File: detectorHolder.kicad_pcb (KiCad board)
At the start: 2 copper layers, 58.8 x 83 mm, 46 parts, among them J1 Conn_01x03, J2 Conn_02x02_Odd_Even

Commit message: PCBWAY production files (20210110)
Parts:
- removed the H1 at (135.0, 151.9)
- removed the H1 at (104.0, 151.9)
- removed the H1 at (135.0, 122.9)
- removed the H1 at (104.0, 122.9)
- removed the H1 at (135.0, 93.9)
- removed the H2 at (135.0, 170.9)
- removed the H2 at (104.0, 170.9)
- removed the H2 at (135.0, 141.9)
- removed the H2 at (104.0, 141.9)
- removed the H2 at (135.0, 112.9)
- removed the H3 at (156.6, 151.9)
- removed the H3 at (125.6, 151.9)
- removed the H3 at (156.6, 122.9)
- removed the H3 at (125.6, 122.9)
- removed the H3 at (156.6, 93.9)
- removed the H4 at (156.6, 170.9)
- removed the H4 at (125.6, 170.9)
- removed the H4 at (156.6, 141.9)
- removed the H4 at (125.6, 141.9)
- removed the H4 at (156.6, 112.9)
- removed the J1 at (135.0, 161.4)
- removed the J1 at (104.0, 161.4)
- removed the J1 at (135.0, 132.4)
- removed the J1 at (104.0, 132.4)
- removed the J1 at (135.0, 103.4)
- removed the J2 at (149.0, 161.4)
- removed the J2 at (118.0, 161.4)
- removed the J2 at (149.0, 132.4)
- removed the J2 at (118.0, 132.4)
- removed the J2 at (149.0, 103.4)
- removed the R1 at (149.0, 167.7)
- removed the R1 at (118.0, 167.7)
- removed the R1 at (149.0, 138.7)
- removed the R1 at (118.0, 138.7)
- removed the R1 at (149.0, 109.7)
- removed REF** (x4): SolderWirePad_1x01_Drill1mm, Connector_Wire:SolderWirePad_1x01_Drill1mm
- added D1: LED RED, LED_SMD:LED_0805_2012Metric, F.Cu at (125.0, 105.4)
- added R2: 330R, Resistor_SMD:R_0805_2012Metric, F.Cu at (125.0, 100.9)
- J1: footprint Connector_Molex:Molex_PicoBlade_53261-0371_1x03-1MP_P1.25mm_Horizontal -> Connector_JST:JST_PH_B3B-PH-SM4-TB_1x03-1MP_P2.00mm_Vertical
- J2: value Conn_02x02_Odd_Even -> MP801
- moved J1 2.50 mm to (106.5, 103.4), turned to 90 degrees
- moved H4 0.81 mm to (125.0, 112.4)
- moved H3 0.77 mm to (125.0, 94.4)
- moved H2 0.74 mm to (104.5, 112.4)
- moved H1 0.71 mm to (104.5, 94.4)
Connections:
- J1 pad 1: +5V -> GND
- J1 pad 3: GND -> +5V
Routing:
- net /SIGNAL: track 94.3 -> 15.1 mm
- net +5V: track 79.5 -> 19.7 mm
- net GND: track 0.00 -> 6.96 mm, vias 0 -> 1
- net Net-(D1-Pad2): track 0.00 -> 2.58 mm
- added copper zone on B.Cu, net GND
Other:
- board size 58.8 x 83 mm -> 27.5 x 25 mm
- board text added: "MoNo^^BREW"
- board text added: "MoNo^^BREW lab. 20210110 artur.a.pozniak@gmail.com"

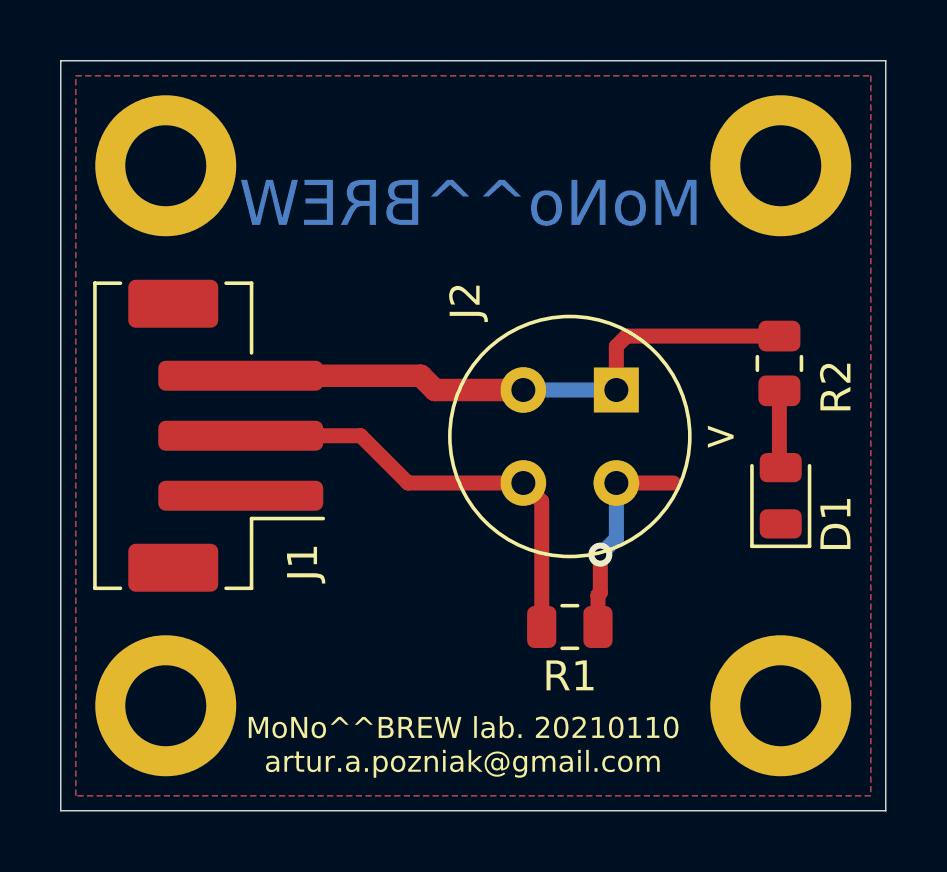
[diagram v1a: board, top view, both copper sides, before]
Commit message: Sensor filpped. Production files (PCBWAY)
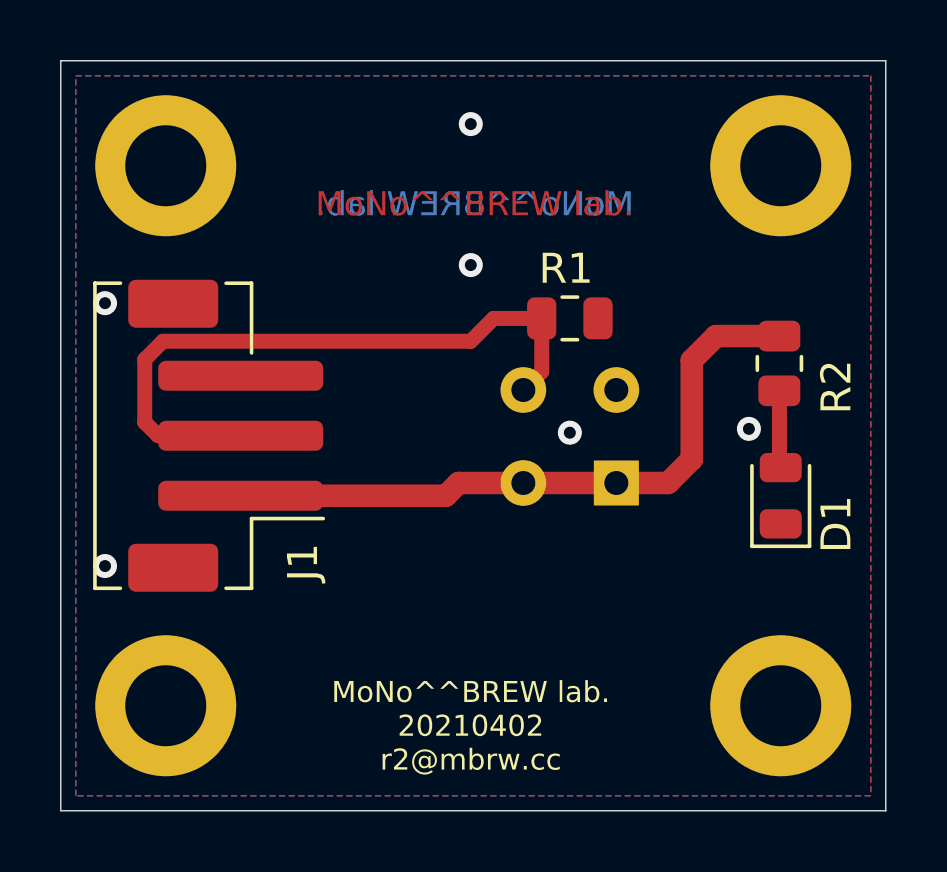
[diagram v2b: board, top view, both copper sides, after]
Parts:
- J2: moved to B.Cu
- moved R1 10.3 mm to (118.0, 99.4)
- turned J2 to 90 degrees
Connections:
- J1 pad 1: GND -> +5V
- J1 pad 3: +5V -> GND
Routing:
- net GND: track 6.96 -> 0.00 mm, vias 1 -> 5
- net /SIGNAL: track 15.1 -> 21.9 mm
- net +5V: track 19.7 -> 22.1 mm
- net (no net): vias 0 -> 1
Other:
- rule pad_to_mask_clearance: 0.051 -> 0
- board text added: "MoNo^^BREW lab."
- board text added: "MoNo^^BREW lab. 20210402 r2@mbrw.cc"
- board text removed: "MoNo^^BREW"
- board text removed: "MoNo^^BREW lab. 20210110 artur.a.pozniak@gmail.com"
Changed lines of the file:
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@@
   (general
     (thickness 1.6)
-    (drawings 7)
-    (tracks 21)
+    (drawings 8)
+    (tracks 26)
     (zones 0)
     (modules 9)
@@
     (pad_size 2.49936 2.49936)
     (pad_drill 1.00076)
-    (pad_to_mask_clearance 0.051)
-    (solder_mask_min_width 0.25)
+    (pad_to_mask_clearance 0)
     (aux_axis_origin 116.433 162.928)
     (grid_origin 104.013 93.853)
@@
       (drillshape 0)
       (scaleselection 1)
-      (outputdirectory "PRODUCTION_PCBWAY_20210110"))
+      (outputdirectory "HOLDER_SMOKE_PCBWAY_20210110"))
   )
   (net 0 "")
@@
       (effects (font (size 0.5 0.5) (thickness 0.08)))
     )
-    (pad 2 smd roundrect (at 0.9125 0 90) (size 1.025 1.4) (layers F.Cu F.Paste F.Mask) (roundrect_rratio 0.2439014634146341)
+    (pad 2 smd roundrect (at 0.9125 0 90) (size 1.025 1.4) (layers F.Cu F.Paste F.Mask) (roundrect_rratio 0.2439004878048781)
       (net 3 +5V))
-    (pad 1 smd roundrect (at -0.9125 0 90) (size 1.025 1.4) (layers F.Cu F.Paste F.Mask) (roundrect_rratio 0.2439014634146341)
+    (pad 1 smd roundrect (at -0.9125 0 90) (size 1.025 1.4) (layers F.Cu F.Paste F.Mask) (roundrect_rratio 0.2439004878048781)
       (net 4 "Net-(D1-Pad2)"))
     (model ${KISYS3DMOD}/Resistor_SMD.3dshapes/R_0805_2012Metric.wrl
@@
     (pad MP smd roundrect (at -4.4 -1.75 90) (size 1.6 3) (layers F.Cu F.Paste F.Mask) (roundrect_rratio 0.15625))
     (pad 3 smd roundrect (at 2 0.5 90) (size 1 5.5) (layers F.Cu F.Paste F.Mask) (roundrect_rratio 0.25)
-      (net 3 +5V))
+      (net 1 GND))
     (pad 2 smd roundrect (at 0 0.5 90) (size 1 5.5) (layers F.Cu F.Paste F.Mask) (roundrect_rratio 0.25)
       (net 2 /SIGNAL))
     (pad 1 smd roundrect (at -2 0.5 90) (size 1 5.5) (layers F.Cu F.Paste F.Mask) (roundrect_rratio 0.25)
-      (net 1 GND))
+      (net 3 +5V))
     (model ${KISYS3DMOD}/Connector_JST.3dshapes/JST_PH_B3B-PH-SM4-TB_1x03-1MP_P2.00mm_Vertical.wrl
       (at (xyz 0 0 0))
@@
   )
   (module Resistor_SMD:R_0805_2012Metric (layer F.Cu)
-    (at 117.983 109.728 180)
+    (at 117.983 99.441 180)
     (descr "Resistor SMD 0805 (2012 Metric), square (rectangular) end terminal, IPC_7351 nominal, (Body size source: https://docs.google.com/spreadsheets/d/1BsfQQcO9C6DZCsRaXUlFlo91Tg2WpOkGARC1WS5S8t0/edit?usp=sharing), generated with kicad-footprint-generator")
     (tags resistor)
     (attr smd)
-    (fp_text reference R1 (at 0 -1.65) (layer F.SilkS)
+    (fp_text reference R1 (at 0.127 1.651) (layer F.SilkS)
       (effects (font (size 1 1) (thickness 0.15)))
     )
@@
     )
   )
-  (module RESPIRECO:MP801 (layer F.Cu)
-    (at 117.983 103.378 270)
-    (fp_text reference J2 (at -4.525 3.47 90) (layer F.SilkS)
-      (effects (font (size 1 1) (thickness 0.15)))
-    )
-    (fp_text value MP801 (at 0 -0.5 90) (layer F.Fab)
-      (effects (font (size 1 1) (thickness 0.15)))
-    )
-    (fp_circle (center 0 0) (end 4 0) (layer F.SilkS) (width 0.12))
-    (fp_circle (center 0 0) (end 4.7 0) (layer F.CrtYd) (width 0.1))
-    (pad 4 thru_hole circle (at 1.55 1.55 270) (size 1.524 1.524) (drill 0.8) (layers *.Cu *.Mask)
+  (module RESPIRECO:MP801 (layer B.Cu)
+    (at 117.983 103.378 90)
+    (fp_text reference J2 (at -4.525 -3.47 270) (layer B.SilkS)
+      (effects (font (size 1 1) (thickness 0.15)) (justify mirror))
+    )
+    (fp_text value MP801 (at 0 0.5 270) (layer B.Fab)
+      (effects (font (size 1 1) (thickness 0.15)) (justify mirror))
+    )
+    (fp_circle (center 0 0) (end 4 0) (layer B.SilkS) (width 0.12))
+    (fp_circle (center 0 0) (end 4.7 0) (layer B.CrtYd) (width 0.1))
+    (pad 4 thru_hole circle (at 1.55 -1.55 90) (size 1.524 1.524) (drill 0.8) (layers *.Cu *.Mask)
       (net 2 /SIGNAL))
-    (pad 3 thru_hole circle (at -1.55 1.55 270) (size 1.524 1.524) (drill 0.8) (layers *.Cu *.Mask)
+    (pad 3 thru_hole circle (at -1.55 -1.55 90) (size 1.524 1.524) (drill 0.8) (layers *.Cu *.Mask)
       (net 3 +5V))
-    (pad 2 thru_hole circle (at 1.55 -1.55 270) (size 1.524 1.524) (drill 0.8) (layers *.Cu *.Mask)
+    (pad 2 thru_hole circle (at 1.55 1.55 90) (size 1.524 1.524) (drill 0.8) (layers *.Cu *.Mask)
       (net 1 GND))
-    (pad 1 thru_hole rect (at -1.55 -1.55 270) (size 1.5 1.5) (drill 0.8) (layers *.Cu *.Mask)
+    (pad 1 thru_hole rect (at -1.55 1.55 90) (size 1.5 1.5) (drill 0.8) (layers *.Cu *.Mask)
       (net 3 +5V))
   )
-  (gr_text MoNo^^BREW (at 114.681 95.631) (layer B.Cu)
-    (effects (font (size 1.5 1.5) (thickness 0.3)) (justify mirror))
-  )
-  (gr_text "MoNo^^BREW lab. 20210110\nartur.a.pozniak@gmail.com" (at 114.427 113.665) (layer F.SilkS)
+  (gr_text "MoNo^^BREW lab." (at 114.808 95.631) (layer F.Cu)
+    (effects (font (size 0.8 0.8) (thickness 0.1)))
+  )
+  (gr_text "MoNo^^BREW lab." (at 114.808 95.631) (layer B.Cu)
+    (effects (font (size 0.8 0.8) (thickness 0.1)) (justify mirror))
+  )
+  (gr_text "MoNo^^BREW lab.\n20210402\nr2@mbrw.cc" (at 114.681 113.03) (layer F.SilkS)
     (effects (font (size 0.7 0.7) (thickness 0.08)))
   )
-  (gr_text > (at 123.013 103.353) (layer F.SilkS)
-    (effects (font (size 1 1) (thickness 0.15)))
+  (gr_text > (at 123.013 103.251 180) (layer B.SilkS)
+    (effects (font (size 1 1) (thickness 0.15)) (justify mirror))
   )
   (gr_line (start 101.013 115.853) (end 101.013 90.853) (layer Edge.Cuts) (width 0.05))
@@
   (gr_line (start 128.513 90.853) (end 128.513 115.853) (layer Edge.Cuts) (width 0.05))
   (gr_line (start 101.013 90.853) (end 128.513 90.853) (layer Edge.Cuts) (width 0.05))
-  (via (at 118.999 107.315) (size 0.8) (drill 0.4) (layers F.Cu B.Cu) (net 1))
-  (segment (start 119.533 106.781) (end 118.999 107.315) (width 0.5) (layer B.Cu) (net 1))
-  (segment (start 119.533 104.928) (end 119.533 106.781) (width 0.5) (layer B.Cu) (net 1))
-  (segment (start 118.999 107.315) (end 118.999 108.585) (width 0.5) (layer F.Cu) (net 1))
-  (segment (start 118.9205 108.6635) (end 118.9205 109.728) (width 0.5) (layer F.Cu) (net 1))
-  (segment (start 118.999 108.585) (end 118.9205 108.6635) (width 0.5) (layer F.Cu) (net 1))
-  (segment (start 119.533 104.928) (end 121.438 104.928) (width 0.5) (layer F.Cu) (net 1))
-  (segment (start 117.0455 105.5405) (end 116.433 104.928) (width 0.5) (layer F.Cu) (net 2))
-  (segment (start 117.0455 109.728) (end 117.0455 105.5405) (width 0.5) (layer F.Cu) (net 2))
-  (segment (start 112.588 104.928) (end 116.433 104.928) (width 0.5) (layer F.Cu) (net 2))
-  (segment (start 111.013 103.353) (end 112.588 104.928) (width 0.5) (layer F.Cu) (net 2))
-  (segment (start 107.013 103.353) (end 111.013 103.353) (width 0.5) (layer F.Cu) (net 2))
-  (segment (start 107.013 101.353) (end 113.013 101.353) (width 0.75) (layer F.Cu) (net 3))
-  (segment (start 113.013 101.353) (end 113.488 101.828) (width 0.75) (layer F.Cu) (net 3))
-  (segment (start 113.488 101.828) (end 116.433 101.828) (width 0.75) (layer F.Cu) (net 3))
-  (segment (start 119.533 101.828) (end 119.533 100.373) (width 0.5) (layer F.Cu) (net 3) (status 1000000))
-  (segment (start 119.8755 100.0305) (end 124.968 100.0305) (width 0.5) (layer F.Cu) (net 3) (status 1000000))
-  (segment (start 119.533 100.373) (end 119.8755 100.0305) (width 0.5) (layer F.Cu) (net 3) (status 1000000))
-  (segment (start 116.433 101.828) (end 119.533 101.828) (width 0.5) (layer B.Cu) (net 3))
+  (via (at 114.681 97.663) (size 0.8) (drill 0.4) (layers F.Cu B.Cu) (net 0))
+  (via (at 102.489 98.933) (size 0.8) (drill 0.4) (layers F.Cu B.Cu) (net 1))
+  (via (at 102.489 107.696) (size 0.8) (drill 0.4) (layers F.Cu B.Cu) (net 1))
+  (via (at 117.983 103.251) (size 0.8) (drill 0.4) (layers F.Cu B.Cu) (net 1))
+  (via (at 114.681 92.964) (size 0.8) (drill 0.4) (layers F.Cu B.Cu) (net 1))
+  (via (at 123.952 103.124) (size 0.8) (drill 0.4) (layers F.Cu B.Cu) (net 1))
+  (segment (start 117.0455 101.2155) (end 116.433 101.828) (width 0.5) (layer F.Cu) (net 2))
+  (segment (start 117.0455 99.441) (end 117.0455 101.2155) (width 0.5) (layer F.Cu) (net 2))
+  (segment (start 103.81299 100.813044) (end 104.423024 100.20301) (width 0.5) (layer F.Cu) (net 2))
+  (segment (start 103.81299 102.90299) (end 103.81299 100.813044) (width 0.5) (layer F.Cu) (net 2))
+  (segment (start 104.263 103.353) (end 103.81299 102.90299) (width 0.5) (layer F.Cu) (net 2))
+  (segment (start 104.423024 100.20301) (end 114.68099 100.20301) (width 0.5) (layer F.Cu) (net 2))
+  (segment (start 107.013 103.353) (end 104.263 103.353) (width 0.5) (layer F.Cu) (net 2))
+  (segment (start 115.443 99.441) (end 117.0455 99.441) (width 0.5) (layer F.Cu) (net 2))
+  (segment (start 114.68099 100.20301) (end 115.443 99.441) (width 0.5) (layer F.Cu) (net 2))
+  (segment (start 107.013 105.353) (end 113.849 105.353) (width 0.75) (layer F.Cu) (net 3))
+  (segment (start 114.274 104.928) (end 116.433 104.928) (width 0.75) (layer F.Cu) (net 3))
+  (segment (start 113.849 105.353) (end 114.274 104.928) (width 0.75) (layer F.Cu) (net 3))
+  (segment (start 116.433 104.928) (end 119.533 104.928) (width 0.75) (layer F.Cu) (net 3))
+  (segment (start 122.8545 100.0305) (end 124.968 100.0305) (width 0.75) (layer F.Cu) (net 3))
+  (segment (start 122.047 100.838) (end 122.8545 100.0305) (width 0.75) (layer F.Cu) (net 3))
+  (segment (start 122.047 104.14) (end 122.047 100.838) (width 0.75) (layer F.Cu) (net 3))
+  (segment (start 121.259 104.928) (end 122.047 104.14) (width 0.75) (layer F.Cu) (net 3))
+  (segment (start 119.533 104.928) (end 121.259 104.928) (width 0.75) (layer F.Cu) (net 3))
   (segment (start 124.968 104.3705) (end 125.013 104.4155) (width 0.5) (layer F.Cu) (net 4))
   (segment (start 124.968 101.8555) (end 124.968 104.3705) (width 0.5) (layer F.Cu) (net 4))
